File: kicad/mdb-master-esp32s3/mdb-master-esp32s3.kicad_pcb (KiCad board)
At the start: 2 copper layers, 40 x 46 mm, 36 parts, among them J1 Conn_02x11_Odd_Even, J2 USB_C_Receptacle_USB2.0_16P, J3 MDB_Connector, J4 Barrel_Jack, Q1 BC807, SW1 SW_Push, U1 ESP32-S3FH4R2, U2 LM2594HVM-3.3, Y1 Crystal_GND24

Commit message: Routing...
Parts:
- moved C10 42.8 mm to (144.4, 90.2), turned to -90 degrees
- moved R1 41.7 mm to (138.2, 90.8), turned to 180 degrees
- moved R7 38.0 mm to (138.2, 93.9)
- moved TP2 33.5 mm to (156.9, 96.8)
- moved C8 31.5 mm to (149.1, 90.2), turned to -90 degrees
- moved C9 28.4 mm to (152.6, 96.7), turned to 180 degrees
- moved TP1 23.5 mm to (157.7, 113.6)
- moved R9 18.3 mm to (135.8, 77.4)
- moved Q1 18.3 mm to (131.3, 78.5), turned to 90 degrees
- moved R8 17.2 mm to (135.8, 80.7), turned to 90 degrees
- moved D1 14.8 mm to (160.1, 93.3), turned to -90 degrees
- moved C11 9.77 mm to (162.3, 93.3), turned to -90 degrees
- moved R5 7.88 mm to (135.8, 110.0)
- moved R6 7.84 mm to (135.8, 106.3)
- moved U2 7.83 mm to (161.9, 110.5), turned to 90 degrees
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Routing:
- net GND: track 0.00 -> 187.8 mm, vias 0 -> 5
- net +3V3: track 0.00 -> 123.8 mm, vias 0 -> 4
- net /vin: track 0.00 -> 87.2 mm, vias 0 -> 1
- net /boot: track 0.00 -> 45.7 mm, vias 0 -> 2
- net /io21: track 0.00 -> 38.9 mm, vias 0 -> 2
- net /u0txd: track 0.00 -> 33.6 mm, vias 0 -> 1
- net /u0rxd: track 0.00 -> 32.7 mm, vias 0 -> 1
- net /reset: track 0.00 -> 31.9 mm
- net /io5: track 0.00 -> 29.3 mm, vias 0 -> 1
- net /io4: track 0.00 -> 26.9 mm, vias 0 -> 1
- net /mdb_master_transmit: track 0.00 -> 16.5 mm
- net /io8: track 0.00 -> 16.2 mm
- net /io18: track 0.00 -> 15.5 mm
- net /io1: track 0.00 -> 15.4 mm, vias 0 -> 1
- net Net-(U1-XTAL_N): track 0.00 -> 14.6 mm
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- added copper zone on F.Cu, net GND
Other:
- board size 40 x 46 mm -> 39 x 40 mm
- board text added: "0_"
- board text added: "3v3"
- board text removed: "+3v3"
- board text removed: "0"

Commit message: Routing
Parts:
- added REF**: OSHW-Logo2_14.6x12mm_SilkScreen, Symbol:OSHW-Logo2_14.6x12mm_SilkScreen, B.Cu at (156.0, 107.0)
- moved C4 3.01 mm to (156.8, 89.6), turned to 90 degrees
- moved C5 1.70 mm to (150.5, 90.2)
- moved Y1 1.68 mm to (153.6, 89.9)
- moved C8 1.36 mm to (147.8, 90.2)
- moved TP2 0.60 mm to (157.5, 96.8), turned to 90 degrees
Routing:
- net Net-(U1-XTAL_P): track 10.3 -> 8.62 mm
- net /vin: track 87.2 -> 86.1 mm
- net +3V3: track 123.8 -> 122.8 mm
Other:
- board text added: "VMflow.xyz"
- board text added: "mdb-controller-esp32s3"
- board text removed: "mdb-master-esp32s3"

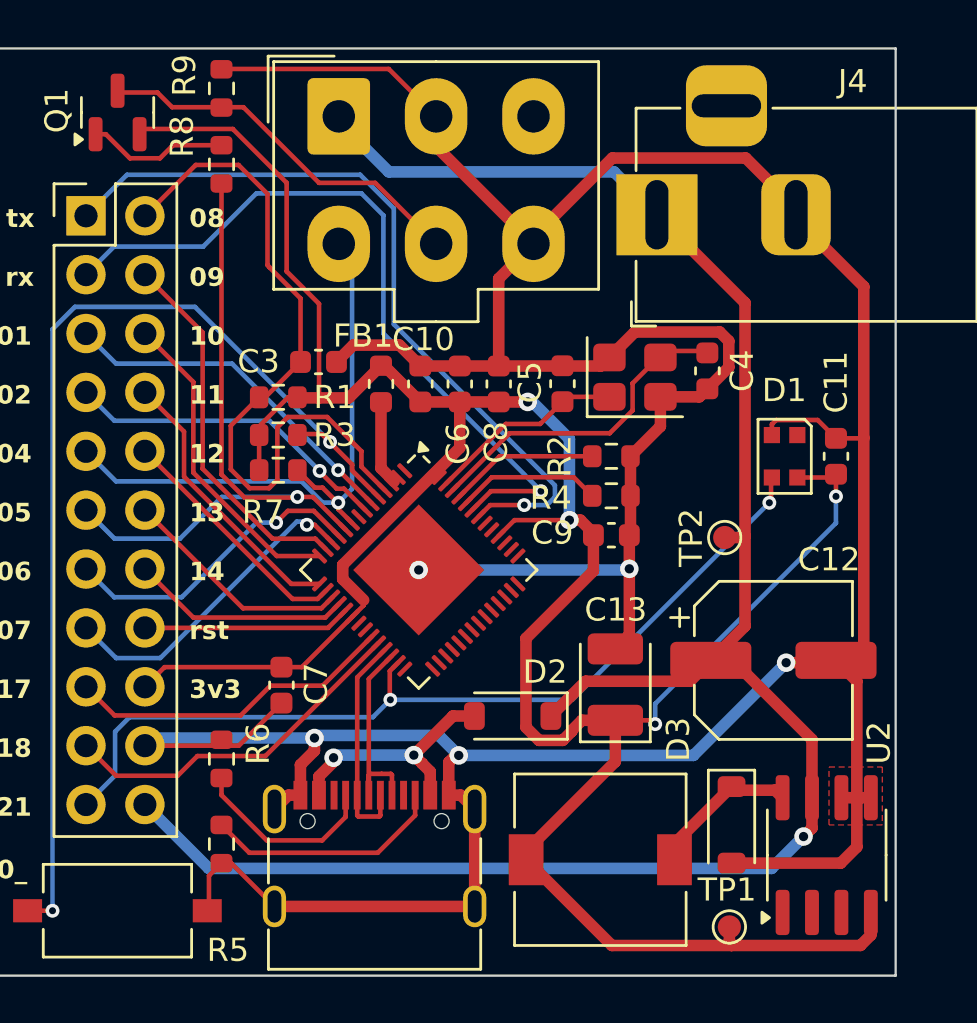
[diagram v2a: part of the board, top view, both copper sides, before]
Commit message: Refacting production components
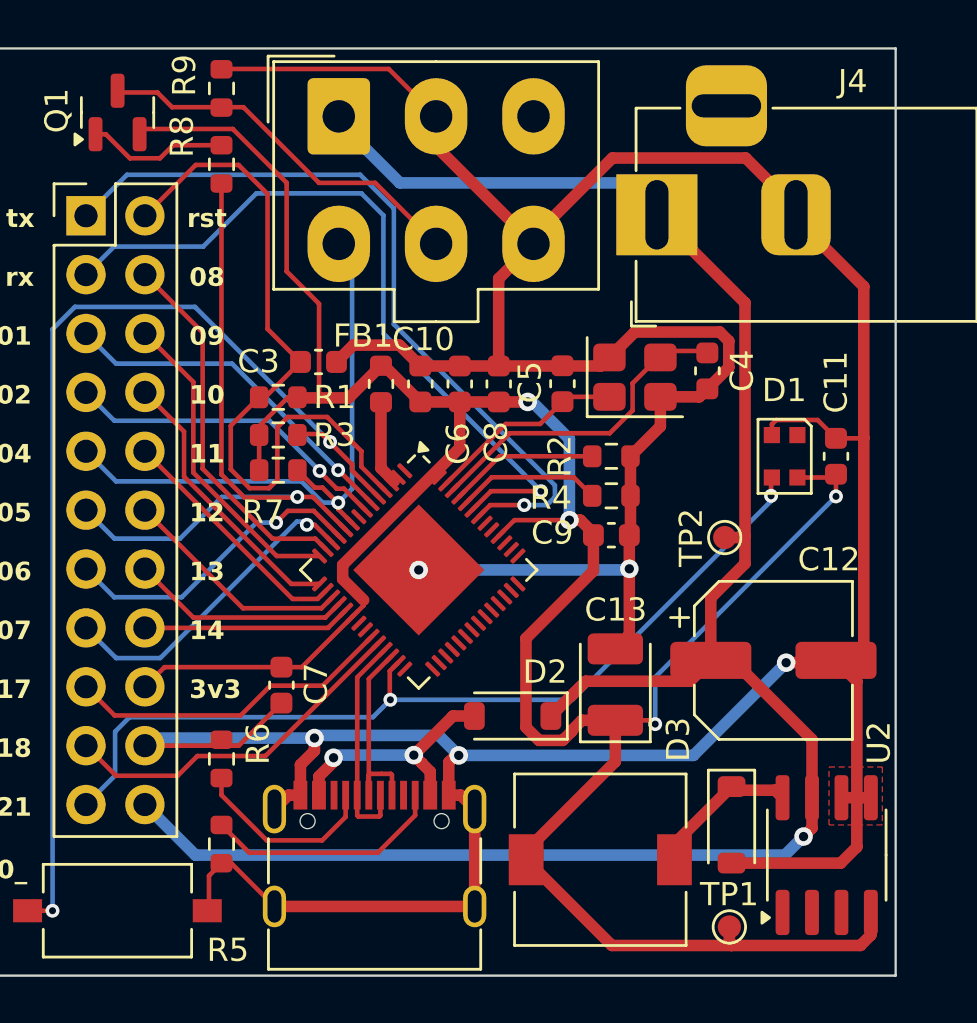
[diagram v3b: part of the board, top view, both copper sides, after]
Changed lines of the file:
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@@
 		(tags "test point SMD pad")
 		(property "Reference" "TP1"
-			(at -0.1 -1.6 0)
+			(at 0 -1.4 0)
 			(layer "F.SilkS")
 			(effects
@@
 		(tags "LED RGB NeoPixel Nano PLCC-4 2020")
 		(property "Reference" "D1"
-			(at -2.845 0.015 180)
+			(at -2.845 0.015 0)
 			(layer "F.SilkS")
 			(effects
@@
 			)
 			(scale
-				(xyz 1.6 1 1)
+				(xyz 1.7 1 1.3)
 			)
 			(rotate
@@
 	)
 	(gr_text "10"
-		(at 134.4 88.58 0)
+		(at 134.4 91.12 0)
 		(layer "F.SilkS" knockout)
 		(effects
@@
 	)
 	(gr_text "11"
-		(at 134.4 91.12 0)
+		(at 134.4 93.66 0)
 		(layer "F.SilkS" knockout)
 		(effects
@@
 	)
 	(gr_text "12"
-		(at 134.4 93.66 0)
+		(at 134.4 96.2 0)
 		(layer "F.SilkS" knockout)
 		(effects
@@
 	)
 	(gr_text "13"
-		(at 134.4 96.2 0)
+		(at 134.4 98.74 0)
 		(layer "F.SilkS" knockout)
 		(effects
@@
 	)
 	(gr_text "rst"
-		(at 134.4 101.28 0)
+		(at 134.3 83.5 0)
 		(layer "F.SilkS" knockout)
 		(effects
@@
 	)
 	(gr_text "08"
-		(at 134.4 83.5 0)
+		(at 134.4 86.04 0)
 		(layer "F.SilkS" knockout)
 		(effects
@@
 	)
 	(gr_text "14"
-		(at 134.4 98.74 0)
+		(at 134.4 101.28 0)
 		(layer "F.SilkS" knockout)
 		(effects
@@
 	)
 	(gr_text "09"
-		(at 134.4 86.04 0)
+		(at 134.4 88.58 0)
 		(layer "F.SilkS" knockout)
 		(effects
@@
 	(segment
 		(start 154.5 104.85)
-		(end 154.5 103.975)
-		(width 0.2)
-		(layer "B.Cu")
-		(net 4)
-	)
-	(segment
-		(start 154.5 103.975)
-		(end 162.3 96.175)
+		(end 154.5 102.825)
 		(width 0.2)
 		(layer "B.Cu")
@@
 	)
 	(segment
-		(start 162.3 96.175)
+		(start 154.5 102.825)
 		(end 162.3 95.025)
 		(width 0.2)
@@
 	)
 	(segment
-		(start 159.5 94.245)
-		(end 159.535 94.21)
-		(width 0.2)
-		(layer "F.Cu")
-		(net 7)
-	)
-	(segment
 		(start 143.075 103.8)
 		(end 143.05 103.775)
@@
 	)
 	(segment
-		(start 159.425 95.3)
-		(end 159.5 95.225)
+		(start 159.5 94.245)
+		(end 159.535 94.21)
 		(width 0.2)
 		(layer "F.Cu")
@@
 	)
 	(segment
-		(start 159.5 95.225)
+		(start 159.5 95)
 		(end 159.5 94.245)
 		(width 0.2)
@@
 	)
 	(via
-		(at 159.425 95.3)
+		(at 159.5 95)
 		(size 0.6)
 		(drill 0.3)
@@
 	)
 	(segment
-		(start 159.425 95.3)
-		(end 150.925 103.8)
+		(start 159.5 95)
+		(end 159.5 95.225)
 		(width 0.2)
 		(layer "B.Cu")
@@
 	)
 	(segment
+		(start 159.5 95.225)
+		(end 150.925 103.8)
+		(width 0.2)
+		(layer "B.Cu")
+		(net 7)
+	)
+	(segment
 		(start 131.2 107.063405)
 		(end 131.2 105.175)
@@
 	)
 	(segment
+		(start 156.9 99.4)
+		(end 156.9 102.1)
+		(width 0.5)
+		(layer "F.Cu")
+		(net 9)
+	)
+	(segment
 		(start 158.327 96.8)
 		(end 158.377 96.75)
@@
 	)
 	(segment
-		(start 157.85 102.1)
-		(end 161.265 105.515)
+		(start 158.377 97.923)
+		(end 156.9 99.4)
 		(width 0.5)
 		(layer "F.Cu")
@@
 	)
 	(segment
-		(start 158.377 100.623)
-		(end 156.9 102.1)
+		(start 157.85 102.1)
+		(end 161.265 105.515)
 		(width 0.5)
 		(layer "F.Cu")
@@
 	)
 	(segment
+		(start 158.377 96.75)
+		(end 158.377 97.923)
+		(width 0.5)
+		(layer "F.Cu")
+		(net 9)
+	)
+	(segment
 		(start 156.9 102.1)
 		(end 157.85 102.1)
@@
 	)
 	(segment
-		(start 158.377 96.75)
-		(end 158.377 100.623)
-		(width 0.5)
-		(layer "F.Cu")
-		(net 9)
-	)
-	(segment
 		(start 158.377 86.677)
 		(end 158.377 96.75)
@@
 	)
 	(segment
-		(start 140.85 78.865)
-		(end 143.01 81.025)
+		(start 134.665405 110.5)
+		(end 132.484405 108.319)
 		(width 0.5)
 		(layer "B.Cu")
@@
 	)
 	(segment
-		(start 152.725 81.025)
+		(start 153.2 81.5)
 		(end 154.575 82.875)
 		(width 0.5)
@@
 	)
 	(segment
-		(start 143.01 81.025)
-		(end 152.725 81.025)
+		(start 140.85 78.63)
+		(end 140.85 78.865)
 		(width 0.5)
 		(layer "B.Cu")
@@
 	)
 	(segment
-		(start 140.85 78.63)
-		(end 140.85 78.865)
+		(start 143.485 81.5)
+		(end 153.2 81.5)
 		(width 0.5)
 		(layer "B.Cu")
@@
 	(segment
 		(start 160.9 109.7)
-		(end 159.525 111.075)
+		(end 160.1 110.5)
 		(width 0.5)
 		(layer "B.Cu")
@@
 	)
 	(segment
-		(start 159.525 111.075)
-		(end 135.240405 111.075)
+		(start 160.1 110.5)
+		(end 134.665405 110.5)
 		(width 0.5)
 		(layer "B.Cu")
@@
 	)
 	(segment
-		(start 135.240405 111.075)
-		(end 132.484405 108.319)
+		(start 140.85 78.865)
+		(end 143.485 81.5)
 		(width 0.5)
 		(layer "B.Cu")
@@
 	)
 	(segment
-		(start 134.678405 80.725)
-		(end 136.525 80.725)
-		(width 0.2)
-		(layer "F.Cu")
-		(net 29)
-	)
-	(segment
 		(start 138.651936 91.599)
 		(end 140.349 91.599)
@@
 	)
 	(segment
-		(start 138.2 92.050936)
-		(end 138.651936 91.599)
-		(width 0.2)
-		(layer "F.Cu")
-		(net 29)
-	)
-	(segment
-		(start 137.001936 94.671)
-		(end 137.843 94.671)
+		(start 137.775 87.8)
+		(end 139.2 89.225)
 		(width 0.2)
 		(layer "F.Cu")
@@
 	)
 	(segment
-		(start 137.44 90.775)
-		(end 137.65 90.775)
+		(start 134.678405 80.725)
+		(end 136.525 80.725)
 		(width 0.2)
 		(layer "F.Cu")
@@
 	)
 	(segment
-		(start 137.849 85.1336)
-		(end 139.2 86.4846)
+		(start 138.2 92.050936)
+		(end 138.651936 91.599)
 		(width 0.2)
 		(layer "F.Cu")
@@
 	)
 	(segment
-		(start 137.415 90.75)
-		(end 137.44 90.775)
+		(start 137.001936 94.671)
+		(end 137.843 94.671)
 		(width 0.2)
 		(layer "F.Cu")
@@
 	)
 	(segment
-		(start 137.775 85.05)
-		(end 137.849 85.124)
+		(start 137.44 90.775)
+		(end 137.65 90.775)
 		(width 0.2)
 		(layer "F.Cu")
@@
 	)
 	(segment
-		(start 132.484405 82.919)
-		(end 134.678405 80.725)
+		(start 136.525 80.725)
+		(end 137.775 81.975)
 		(width 0.2)
 		(layer "F.Cu")
@@
 	)
 	(segment
-		(start 139.2 86.4846)
-		(end 139.2 89.225)
+		(start 137.415 90.75)
+		(end 137.44 90.775)
 		(width 0.2)
 		(layer "F.Cu")
@@
 	)
 	(segment
-		(start 136.525 80.725)
-		(end 137.775 81.975)
-		(width 0.2)
-		(layer "F.Cu")
-		(net 29)
-	)
-	(segment
-		(start 137.775 81.975)
-		(end 137.775 85.05)
+		(start 132.484405 82.919)
+		(end 134.678405 80.725)
 		(width 0.2)
 		(layer "F.Cu")
@@
 	)
 	(segment
-		(start 137.849 85.124)
-		(end 137.849 85.1336)
+		(start 140.349 91.599)
+		(end 141.826 93.076)
 		(width 0.2)
 		(layer "F.Cu")
@@
 	)
 	(segment
-		(start 140.349 91.599)
-		(end 141.826 93.076)
+		(start 137.775 81.975)
+		(end 137.775 87.8)
 		(width 0.2)
 		(layer "F.Cu")
